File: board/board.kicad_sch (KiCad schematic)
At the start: 5 parts, among them J1 003_power, J2 Conn_01x02_Male, J3 003_power

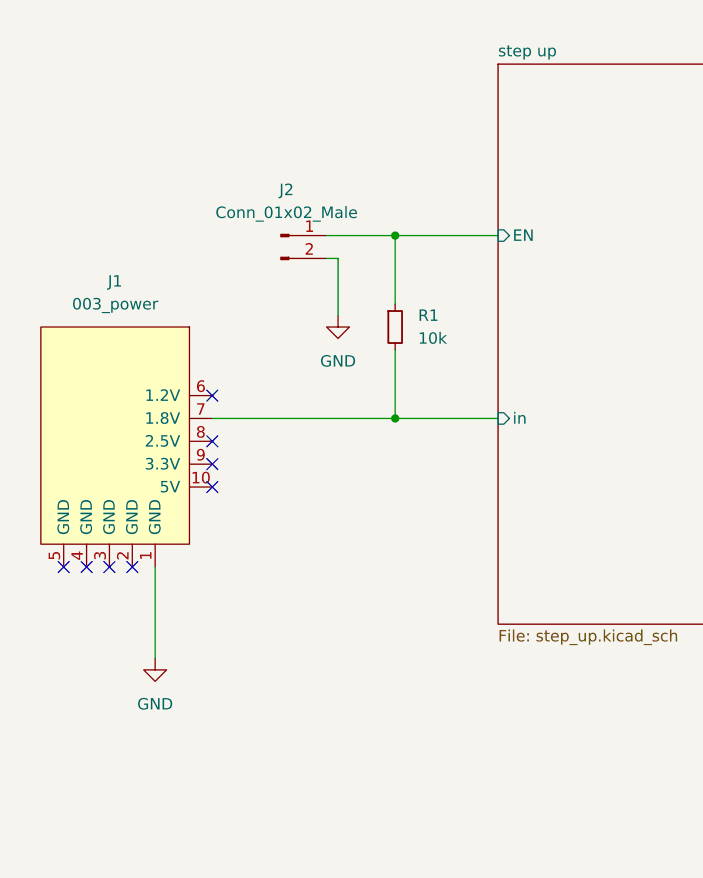
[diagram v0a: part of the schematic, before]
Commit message: moved components for better EMC
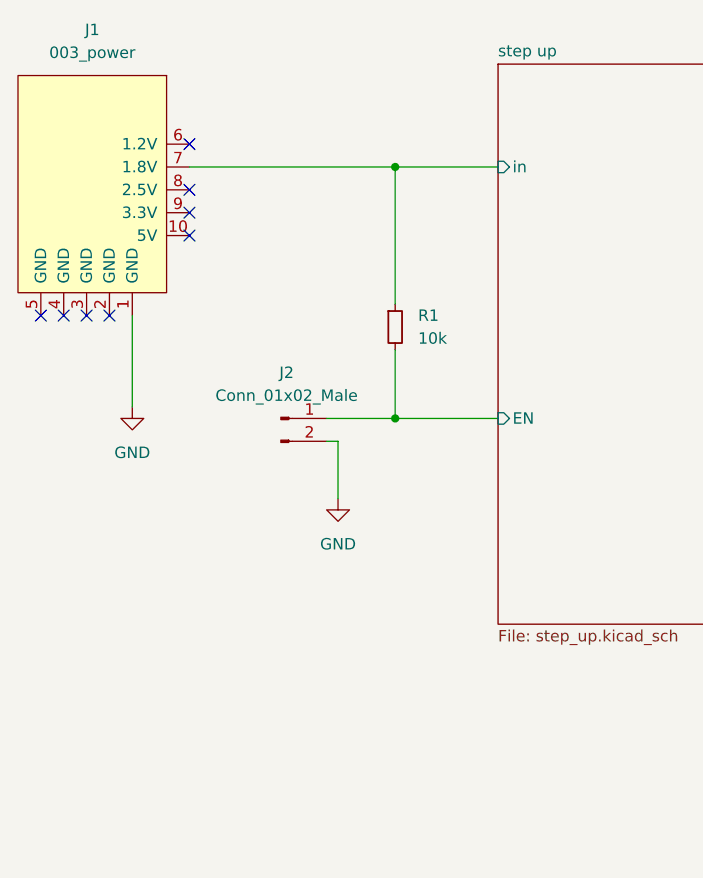
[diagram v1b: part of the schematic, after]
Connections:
- net step up/EN: now also R1.2; no longer R1.1
- net step up/in: now also R1.1; no longer R1.2
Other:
- moved on the sheet: J1, J2
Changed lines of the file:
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@@
 (kicad_sch (version 20211123) (generator eeschema)
   (paper "A4")
+  (junction (at 102.87 83.82) (diameter 0) (color 0 0 0 0)
+  )
   (junction (at 210.82 129.54) (diameter 0) (color 0 0 0 0)
-  )
-  (junction (at 102.87 91.44) (diameter 0) (color 0 0 0 0)
   )
   (junction (at 102.87 111.76) (diameter 0) (color 0 0 0 0)
@@
   (no_connect (at 218.44 125.73))
   (no_connect (at 220.98 125.73))
-  (no_connect (at 73.66 128.27))
-  (no_connect (at 82.55 114.3))
-  (no_connect (at 82.55 116.84))
-  (no_connect (at 82.55 119.38))
-  (no_connect (at 82.55 109.22))
-  (no_connect (at 66.04 128.27))
-  (no_connect (at 68.58 128.27))
-  (no_connect (at 71.12 128.27))
+  (no_connect (at 71.12 100.33))
+  (no_connect (at 80.01 86.36))
+  (no_connect (at 80.01 88.9))
+  (no_connect (at 80.01 91.44))
+  (no_connect (at 80.01 81.28))
+  (no_connect (at 63.5 100.33))
+  (no_connect (at 66.04 100.33))
+  (no_connect (at 68.58 100.33))
   (no_connect (at 213.36 125.73))
   (no_connect (at 215.9 125.73))
@@
     (stroke (width 0) (type default) (color 0 0 0 0))
   )
-  (wire (pts (xy 95.25 91.44) (xy 102.87 91.44))
+  (wire (pts (xy 95.25 111.76) (xy 102.87 111.76))
     (stroke (width 0) (type default) (color 0 0 0 0))
   )
@@
     (stroke (width 0) (type default) (color 0 0 0 0))
   )
-  (wire (pts (xy 96.52 93.98) (xy 96.52 100.33))
-    (stroke (width 0) (type default) (color 0 0 0 0))
-  )
-  (wire (pts (xy 96.52 93.98) (xy 95.25 93.98))
-    (stroke (width 0) (type default) (color 0 0 0 0))
-  )
-  (wire (pts (xy 76.2 128.27) (xy 76.2 138.43))
-    (stroke (width 0) (type default) (color 0 0 0 0))
-  )
-  (wire (pts (xy 82.55 111.76) (xy 102.87 111.76))
+  (wire (pts (xy 96.52 114.3) (xy 96.52 120.65))
+    (stroke (width 0) (type default) (color 0 0 0 0))
+  )
+  (wire (pts (xy 96.52 114.3) (xy 95.25 114.3))
+    (stroke (width 0) (type default) (color 0 0 0 0))
+  )
+  (wire (pts (xy 73.66 100.33) (xy 73.66 110.49))
+    (stroke (width 0) (type default) (color 0 0 0 0))
+  )
+  (wire (pts (xy 80.01 83.82) (xy 102.87 83.82))
     (stroke (width 0) (type default) (color 0 0 0 0))
   )
@@
     (stroke (width 0) (type default) (color 0 0 0 0))
   )
-  (wire (pts (xy 102.87 91.44) (xy 102.87 99.06))
+  (wire (pts (xy 102.87 83.82) (xy 102.87 99.06))
     (stroke (width 0) (type default) (color 0 0 0 0))
   )
@@
     (stroke (width 0) (type default) (color 0 0 0 0))
   )
-  (wire (pts (xy 114.3 91.44) (xy 102.87 91.44))
+  (wire (pts (xy 114.3 83.82) (xy 102.87 83.82))
     (stroke (width 0) (type default) (color 0 0 0 0))
   )
@@
     (pin "2")
   )
-  (symbol (lib_id "put_on_edge:003_power") (at 71.12 114.3 0) (mirror y) (unit 1)
-    (in_bom yes) (on_board yes) (fields_autoplaced)
-    (property "Reference" "J1" (id 0) (at 71.755 96.52 0))
-    (property "Value" "003_power" (id 1) (at 71.755 99.06 0))
-    (property "Footprint" "on_edge:on_edge_2x05_device" (id 2) (at 63.5 97.79 0)
-      (effects (font (size 1.27 1.27)) hide)
-    )
-    (property "Datasheet" "" (id 3) (at 63.5 97.79 0)
+  (symbol (lib_id "put_on_edge:003_power") (at 68.58 86.36 0) (mirror y) (unit 1)
+    (in_bom yes) (on_board yes) (fields_autoplaced)
+    (property "Reference" "J1" (id 0) (at 69.215 68.58 0))
+    (property "Value" "003_power" (id 1) (at 69.215 71.12 0))
+    (property "Footprint" "on_edge:on_edge_2x05_device" (id 2) (at 60.96 69.85 0)
+      (effects (font (size 1.27 1.27)) hide)
+    )
+    (property "Datasheet" "" (id 3) (at 60.96 69.85 0)
       (effects (font (size 1.27 1.27)) hide)
     )
@@
     (pin "1")
   )
-  (symbol (lib_id "power:GND") (at 76.2 138.43 0) (unit 1)
-    (in_bom yes) (on_board yes) (fields_autoplaced)
-    (property "Reference" "#PWR0102" (id 0) (at 76.2 144.78 0)
-      (effects (font (size 1.27 1.27)) hide)
-    )
-    (property "Value" "GND" (id 1) (at 76.2 143.51 0))
-    (property "Footprint" "" (id 2) (at 76.2 138.43 0)
-      (effects (font (size 1.27 1.27)) hide)
-    )
-    (property "Datasheet" "" (id 3) (at 76.2 138.43 0)
+  (symbol (lib_id "power:GND") (at 73.66 110.49 0) (unit 1)
+    (in_bom yes) (on_board yes) (fields_autoplaced)
+    (property "Reference" "#PWR0102" (id 0) (at 73.66 116.84 0)
+      (effects (font (size 1.27 1.27)) hide)
+    )
+    (property "Value" "GND" (id 1) (at 73.66 115.57 0))
+    (property "Footprint" "" (id 2) (at 73.66 110.49 0)
+      (effects (font (size 1.27 1.27)) hide)
+    )
+    (property "Datasheet" "" (id 3) (at 73.66 110.49 0)
       (effects (font (size 1.27 1.27)) hide)
     )
@@
     )
   )
-  (symbol (lib_id "power:GND") (at 96.52 100.33 0) (unit 1)
-    (in_bom yes) (on_board yes) (fields_autoplaced)
-    (property "Reference" "#PWR0103" (id 0) (at 96.52 106.68 0)
-      (effects (font (size 1.27 1.27)) hide)
-    )
-    (property "Value" "GND" (id 1) (at 96.52 105.41 0))
-    (property "Footprint" "" (id 2) (at 96.52 100.33 0)
-      (effects (font (size 1.27 1.27)) hide)
-    )
-    (property "Datasheet" "" (id 3) (at 96.52 100.33 0)
-      (effects (font (size 1.27 1.27)) hide)
-    )
-    (pin "1")
-  )
-  (symbol (lib_id "Connector:Conn_01x02_Male") (at 90.17 91.44 0) (unit 1)
-    (in_bom yes) (on_board yes) (fields_autoplaced)
-    (property "Reference" "J2" (id 0) (at 90.805 86.36 0))
-    (property "Value" "Conn_01x02_Male" (id 1) (at 90.805 88.9 0))
-    (property "Footprint" "Connector_PinHeader_2.54mm:PinHeader_1x02_P2.54mm_Vertical" (id 2) (at 90.17 91.44 0)
-      (effects (font (size 1.27 1.27)) hide)
-    )
-    (property "Datasheet" "~" (id 3) (at 90.17 91.44 0)
+  (symbol (lib_id "power:GND") (at 96.52 120.65 0) (unit 1)
+    (in_bom yes) (on_board yes) (fields_autoplaced)
+    (property "Reference" "#PWR0103" (id 0) (at 96.52 127 0)
+      (effects (font (size 1.27 1.27)) hide)
+    )
+    (property "Value" "GND" (id 1) (at 96.52 125.73 0))
+    (property "Footprint" "" (id 2) (at 96.52 120.65 0)
+      (effects (font (size 1.27 1.27)) hide)
+    )
+    (property "Datasheet" "" (id 3) (at 96.52 120.65 0)
+      (effects (font (size 1.27 1.27)) hide)
+    )
+    (pin "1")
+  )
+  (symbol (lib_id "Connector:Conn_01x02_Male") (at 90.17 111.76 0) (unit 1)
+    (in_bom yes) (on_board yes) (fields_autoplaced)
+    (property "Reference" "J2" (id 0) (at 90.805 106.68 0))
+    (property "Value" "Conn_01x02_Male" (id 1) (at 90.805 109.22 0))
+    (property "Footprint" "Connector_PinHeader_2.54mm:PinHeader_1x02_P2.54mm_Vertical" (id 2) (at 90.17 111.76 0)
+      (effects (font (size 1.27 1.27)) hide)
+    )
+    (property "Datasheet" "~" (id 3) (at 90.17 111.76 0)
       (effects (font (size 1.27 1.27)) hide)
     )
@@
       (effects (font (size 1.27 1.27)) (justify right))
     )
-    (pin "in" input (at 114.3 111.76 180)
-      (effects (font (size 1.27 1.27)) (justify left))
-    )
-    (pin "EN" input (at 114.3 91.44 180)
-      (effects (font (size 1.27 1.27)) (justify left))
-    )
+    (pin "in" input (at 114.3 83.82 180)
+      (effects (font (size 1.27 1.27)) (justify left))
+    )
+    (pin "EN" input (at 114.3 111.76 180)
+      (effects (font (size 1.27 1.27)) (justify left))
+    )

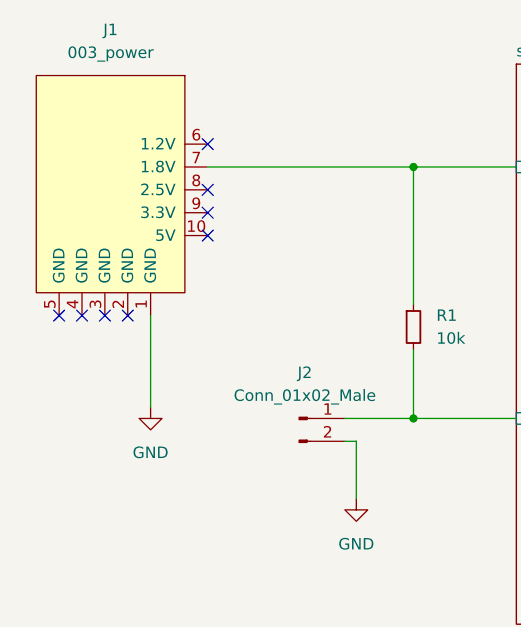
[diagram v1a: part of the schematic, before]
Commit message: changed input to battery cell connector
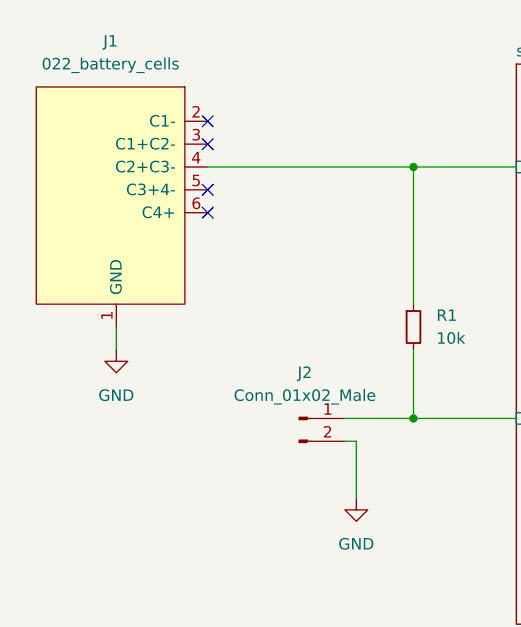
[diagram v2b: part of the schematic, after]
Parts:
- removed J1: 003_power, on_edge:on_edge_2x05_device, symbol put_on_edge:003_power
- added J1: 022_battery_cells, on_edge:on_edge_2x05_device, symbol put_on_edge:022_battery_cells
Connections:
- net GND: now also J1.1 (GND)
- net step up/in: now also J1.4 (C2+C3-)
- no-connect marks 16 -> 12
